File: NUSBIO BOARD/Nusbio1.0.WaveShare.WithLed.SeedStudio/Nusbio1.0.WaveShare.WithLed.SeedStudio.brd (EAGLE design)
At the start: 40.1 x 84 mm, 13 parts

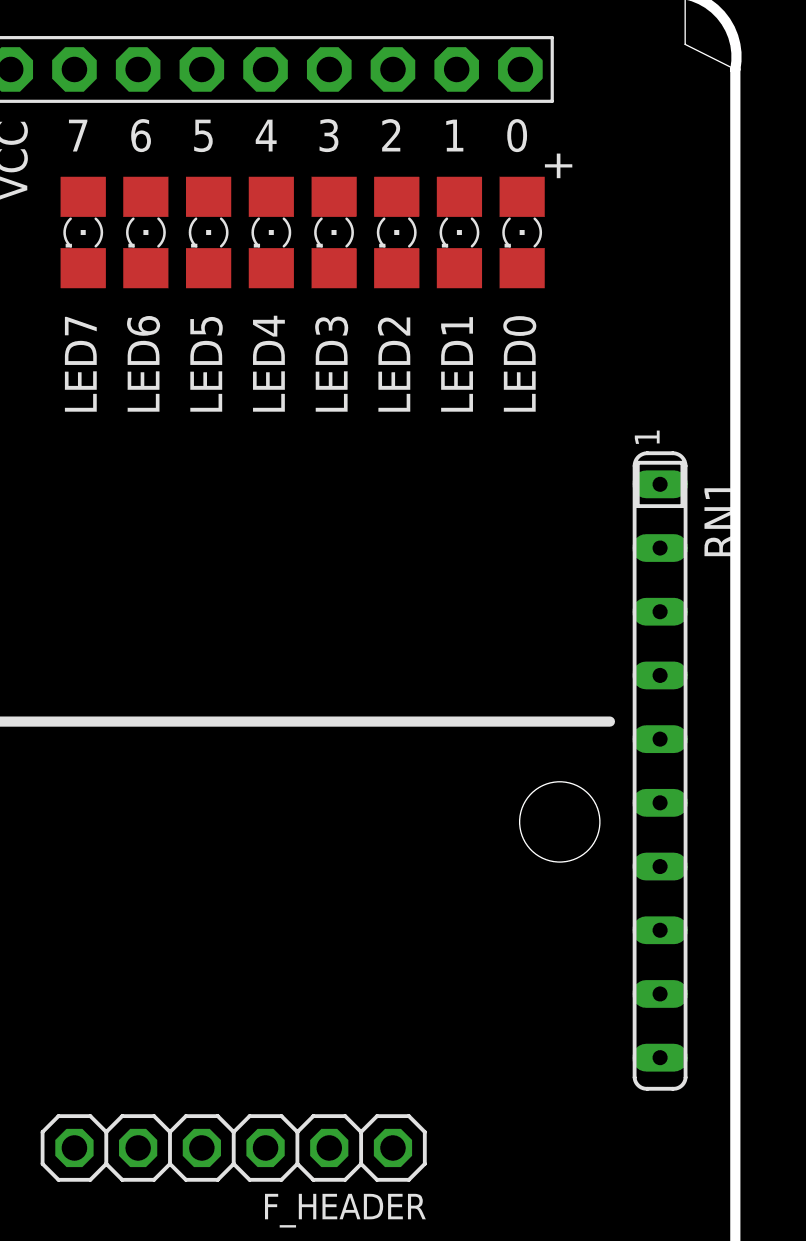
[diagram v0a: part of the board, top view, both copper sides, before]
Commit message: New board Nusbio WaveShare SeedStudio edition larger with 8 blue 1206 led
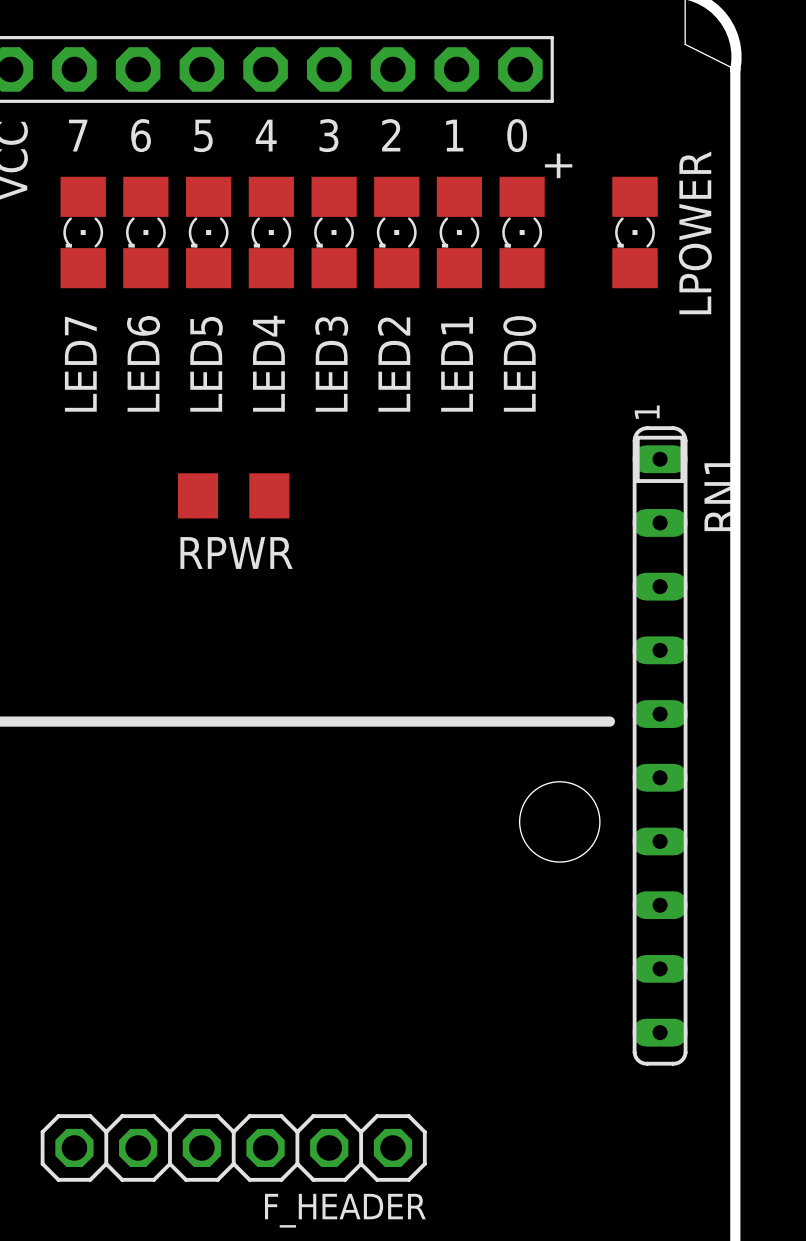
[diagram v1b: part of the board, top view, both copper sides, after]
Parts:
- added LPOWER: (no value), adafruit:1206
- added RPWR: (no value), adafruit:R1206
- moved RN1 1.00 mm to (38.0, 54.0)
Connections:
- new net N$9: LPOWER.C, RPWR.1
- net GND: now also RPWR.2
- net NUSBIO_VCC: now also LPOWER.A
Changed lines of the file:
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@@
 <attribute name="VALUE" x="32.175" y="1.65" size="1.27" layer="27" rot="R90"/>
 </element>
-<element name="RN1" library="resistor-sip" package="SIP10" value="" x="38" y="53" rot="R270"/>
+<element name="RN1" library="resistor-sip" package="SIP10" value="" x="38" y="54" rot="R270"/>
 <element name="LED0" library="adafruit" package="1206" value="" x="32.5" y="74.5" smashed="yes" rot="R270">
 <attribute name="NAME" x="31.77" y="71.27" size="1.27" layer="25" rot="R270"/>
@@
 <attribute name="VALUE" x="17.46" y="75.77" size="1.27" layer="27" rot="R270"/>
 </element>
+<element name="LPOWER" library="adafruit" package="1206" value="" x="37" y="74.5" smashed="yes" rot="R270">
+<attribute name="NAME" x="38.77" y="77.77" size="1.27" layer="25" rot="R270"/>
+<attribute name="VALUE" x="34.46" y="75.77" size="1.27" layer="27" rot="R270"/>
+</element>
+<element name="RPWR" library="adafruit" package="R1206" value="" x="21" y="64" smashed="yes" rot="R180">
+<attribute name="NAME" x="23.397" y="62.357" size="1.27" layer="25" rot="R180"/>
+<attribute name="VALUE" x="22.397" y="66.413" size="1.27" layer="27" rot="R180"/>
+</element>
 </elements>
 <signals>
@@
 <contactref element="F_HEADER" pad="2"/>
 <contactref element="RN1" pad="1"/>
-<wire x1="24.81" y1="38" x2="38" y2="64.46" width="0" layer="19" extent="1-1"/>
-<wire x1="9.57" y1="81" x2="38" y2="64.46" width="0" layer="19" extent="1-1"/>
+<contactref element="RPWR" pad="2"/>
+<wire x1="19.578" y1="64" x2="38" y2="65.46" width="0" layer="19" extent="1-1"/>
+<wire x1="9.57" y1="81" x2="19.578" y2="64" width="0" layer="19" extent="1-1"/>
+<wire x1="24.81" y1="38" x2="19.578" y2="64" width="0" layer="19" extent="1-1"/>
 </signal>
 <signal name="NUSBIO_VCC">
 <contactref element="U$1" pad="9"/>
 <contactref element="F_HEADER" pad="1"/>
-<wire x1="27.35" y1="38" x2="12.11" y2="81" width="0" layer="19" extent="1-1"/>
+<contactref element="LPOWER" pad="A"/>
+<wire x1="12.11" y1="81" x2="37" y2="75.922" width="0" layer="19" extent="1-1"/>
+<wire x1="27.35" y1="38" x2="37" y2="75.922" width="0" layer="19" extent="1-1"/>
 </signal>
 <signal name="TX_G5">
@@
 <contactref element="LED0" pad="C"/>
 <contactref element="RN1" pad="2"/>
-<wire x1="38" y1="61.92" x2="32.5" y2="73.078" width="0" layer="19" extent="1-1"/>
+<wire x1="38" y1="62.92" x2="32.5" y2="73.078" width="0" layer="19" extent="1-1"/>
 </signal>
 <signal name="N$1">
 <contactref element="LED1" pad="C"/>
 <contactref element="RN1" pad="3"/>
-<wire x1="38" y1="59.38" x2="30" y2="73.078" width="0" layer="19" extent="1-1"/>
+<wire x1="38" y1="60.38" x2="30" y2="73.078" width="0" layer="19" extent="1-1"/>
 </signal>
 <signal name="N$3">
 <contactref element="LED2" pad="C"/>
 <contactref element="RN1" pad="4"/>
-<wire x1="38" y1="56.84" x2="27.5" y2="73.078" width="0" layer="19" extent="1-1"/>
+<wire x1="38" y1="57.84" x2="27.5" y2="73.078" width="0" layer="19" extent="1-1"/>
 </signal>
 <signal name="N$4">
 <contactref element="LED3" pad="C"/>
 <contactref element="RN1" pad="5"/>
-<wire x1="38" y1="54.3" x2="25" y2="73.078" width="0" layer="19" extent="1-1"/>
+<wire x1="38" y1="55.3" x2="25" y2="73.078" width="0" layer="19" extent="1-1"/>
 </signal>
 <signal name="N$5">
 <contactref element="LED4" pad="C"/>
 <contactref element="RN1" pad="6"/>
-<wire x1="38" y1="51.76" x2="22.5" y2="73.078" width="0" layer="19" extent="1-1"/>
+<wire x1="38" y1="52.76" x2="22.5" y2="73.078" width="0" layer="19" extent="1-1"/>
 </signal>
 <signal name="N$6">
 <contactref element="LED7" pad="C"/>
 <contactref element="RN1" pad="9"/>
-<wire x1="38" y1="44.14" x2="15" y2="73.078" width="0" layer="19" extent="1-1"/>
+<wire x1="38" y1="45.14" x2="15" y2="73.078" width="0" layer="19" extent="1-1"/>
 </signal>
 <signal name="N$8">
 <contactref element="LED6" pad="C"/>
 <contactref element="RN1" pad="8"/>
-<wire x1="38" y1="46.68" x2="17.5" y2="73.078" width="0" layer="19" extent="1-1"/>
+<wire x1="38" y1="47.68" x2="17.5" y2="73.078" width="0" layer="19" extent="1-1"/>
 </signal>
 <signal name="N$7">
 <contactref element="LED5" pad="C"/>
 <contactref element="RN1" pad="7"/>
-<wire x1="38" y1="49.22" x2="20" y2="73.078" width="0" layer="19" extent="1-1"/>
+<wire x1="38" y1="50.22" x2="20" y2="73.078" width="0" layer="19" extent="1-1"/>
+</signal>
+<signal name="N$9">
+<contactref element="LPOWER" pad="C"/>
+<contactref element="RPWR" pad="1"/>
+<wire x1="22.422" y1="64" x2="37" y2="73.078" width="0" layer="19" extent="1-1"/>
 </signal>
 </signals>

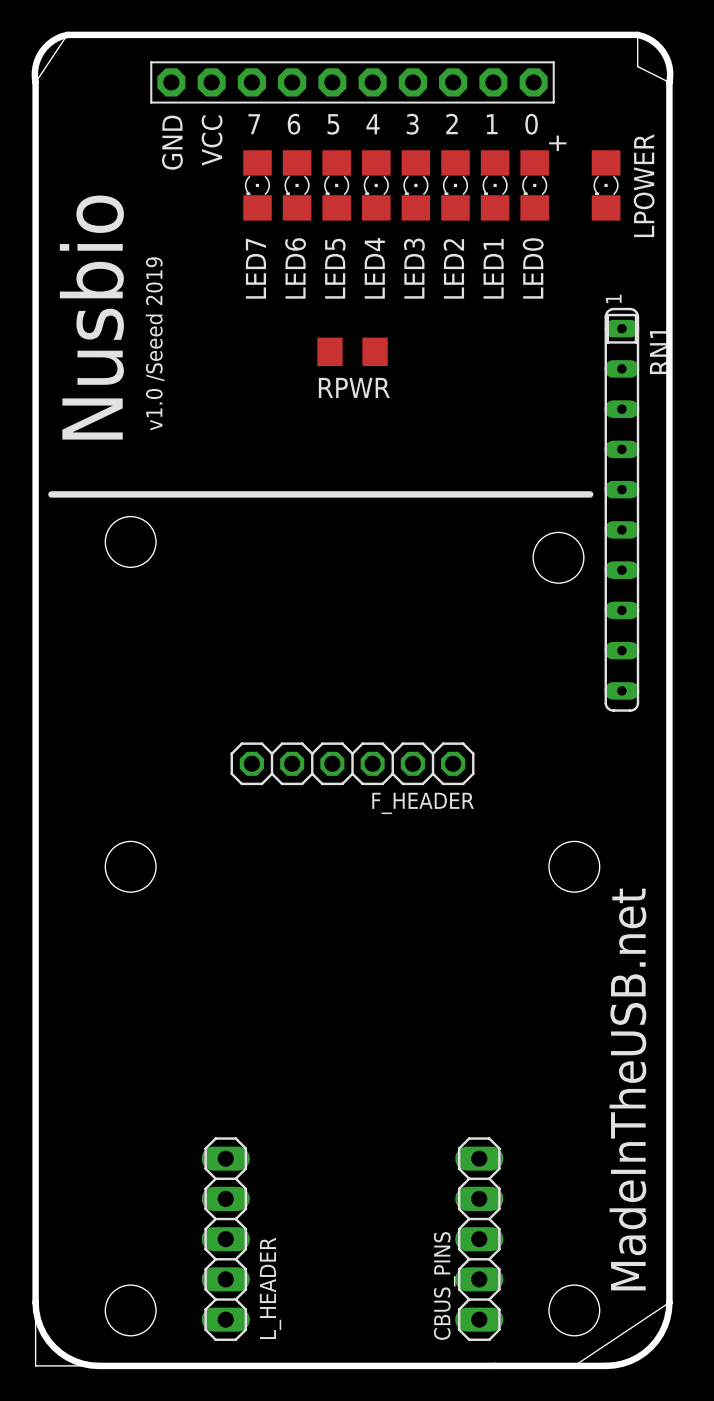
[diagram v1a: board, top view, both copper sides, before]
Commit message: board 4017-7Segment v2 on hold, until I received chip 4017B
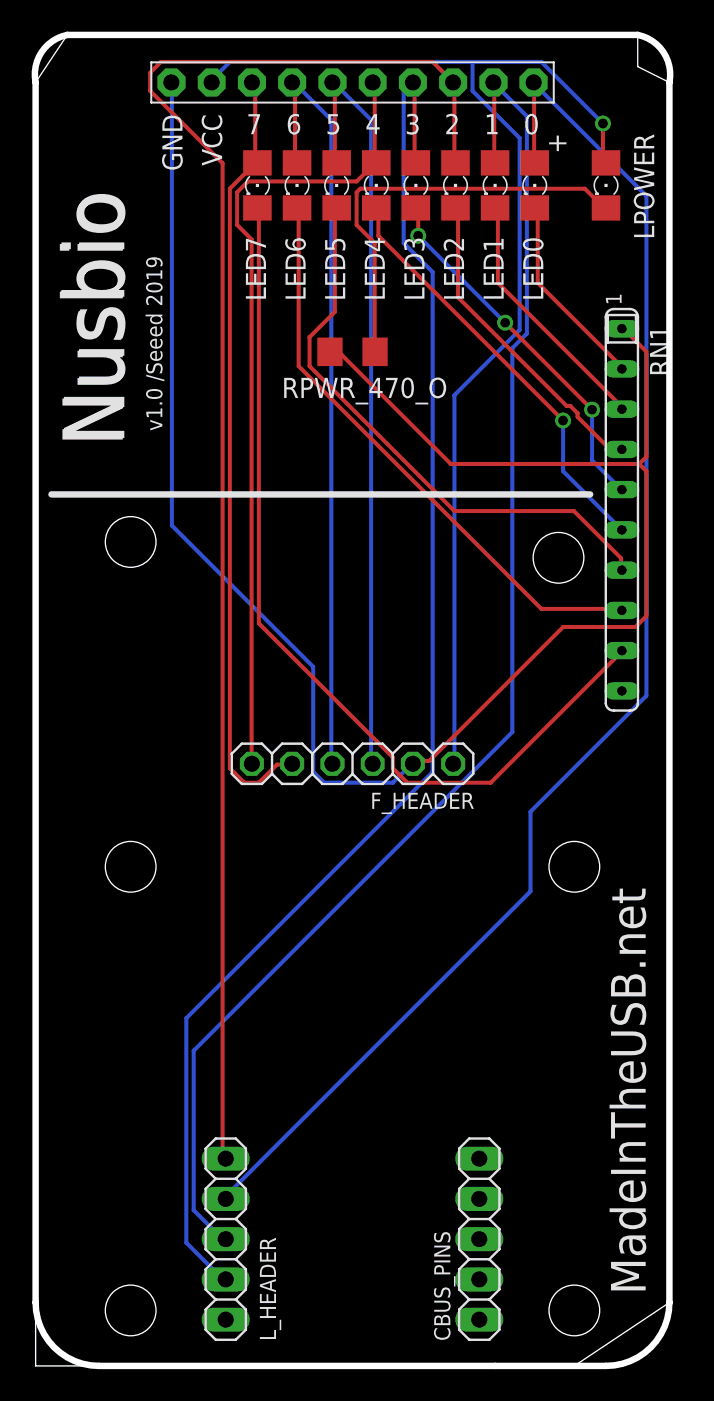
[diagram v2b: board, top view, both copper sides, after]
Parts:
- renumbered RPWR to RPWR_470_O
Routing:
- net GND: track 0.00 -> 114.6 mm
- net DTR_G2: track 0.00 -> 95.6 mm
- net RI_G0: track 0.00 -> 89.5 mm
- net DCD_G3: track 0.00 -> 89.3 mm
- net DSR_G1: track 0.00 -> 88.6 mm
- net NUSBIO_VCC: track 0.00 -> 76.7 mm, vias 0 -> 1
- net N$6: track 0.00 -> 57.2 mm
- net CTS_G4: track 0.00 -> 51.2 mm
- net RX_G6: track 0.00 -> 49.3 mm
- net TX_G5: track 0.00 -> 49.3 mm
- net RTS_G7: track 0.00 -> 49.1 mm
- net N$8: track 0.00 -> 36.8 mm
- net N$7: track 0.00 -> 36.1 mm
- net N$9: track 0.00 -> 26.9 mm
- net N$5: track 0.00 -> 26.7 mm, vias 0 -> 1
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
